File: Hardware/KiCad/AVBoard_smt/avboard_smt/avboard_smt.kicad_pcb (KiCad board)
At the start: 4 copper layers, 177.8 x 152.1 mm, 111 parts, among them IC2_AUD0 7432N, IC36 4040N, IC37 7430N, IC39 7400N, IC40 4040N, IC41 7400N, IC43 7400N, IC44 7486N, IC45 7400N, IC46 74257N, IC47 74257N, IC48 74564N, IC4_AUD0 7400N, IC53 7404N, IC6_AUD0 7474N, IC7_AUD0 LM358N, J1 5V, J2 VID_TO_MOBO, U1 W65C02SP, U2 THS7374

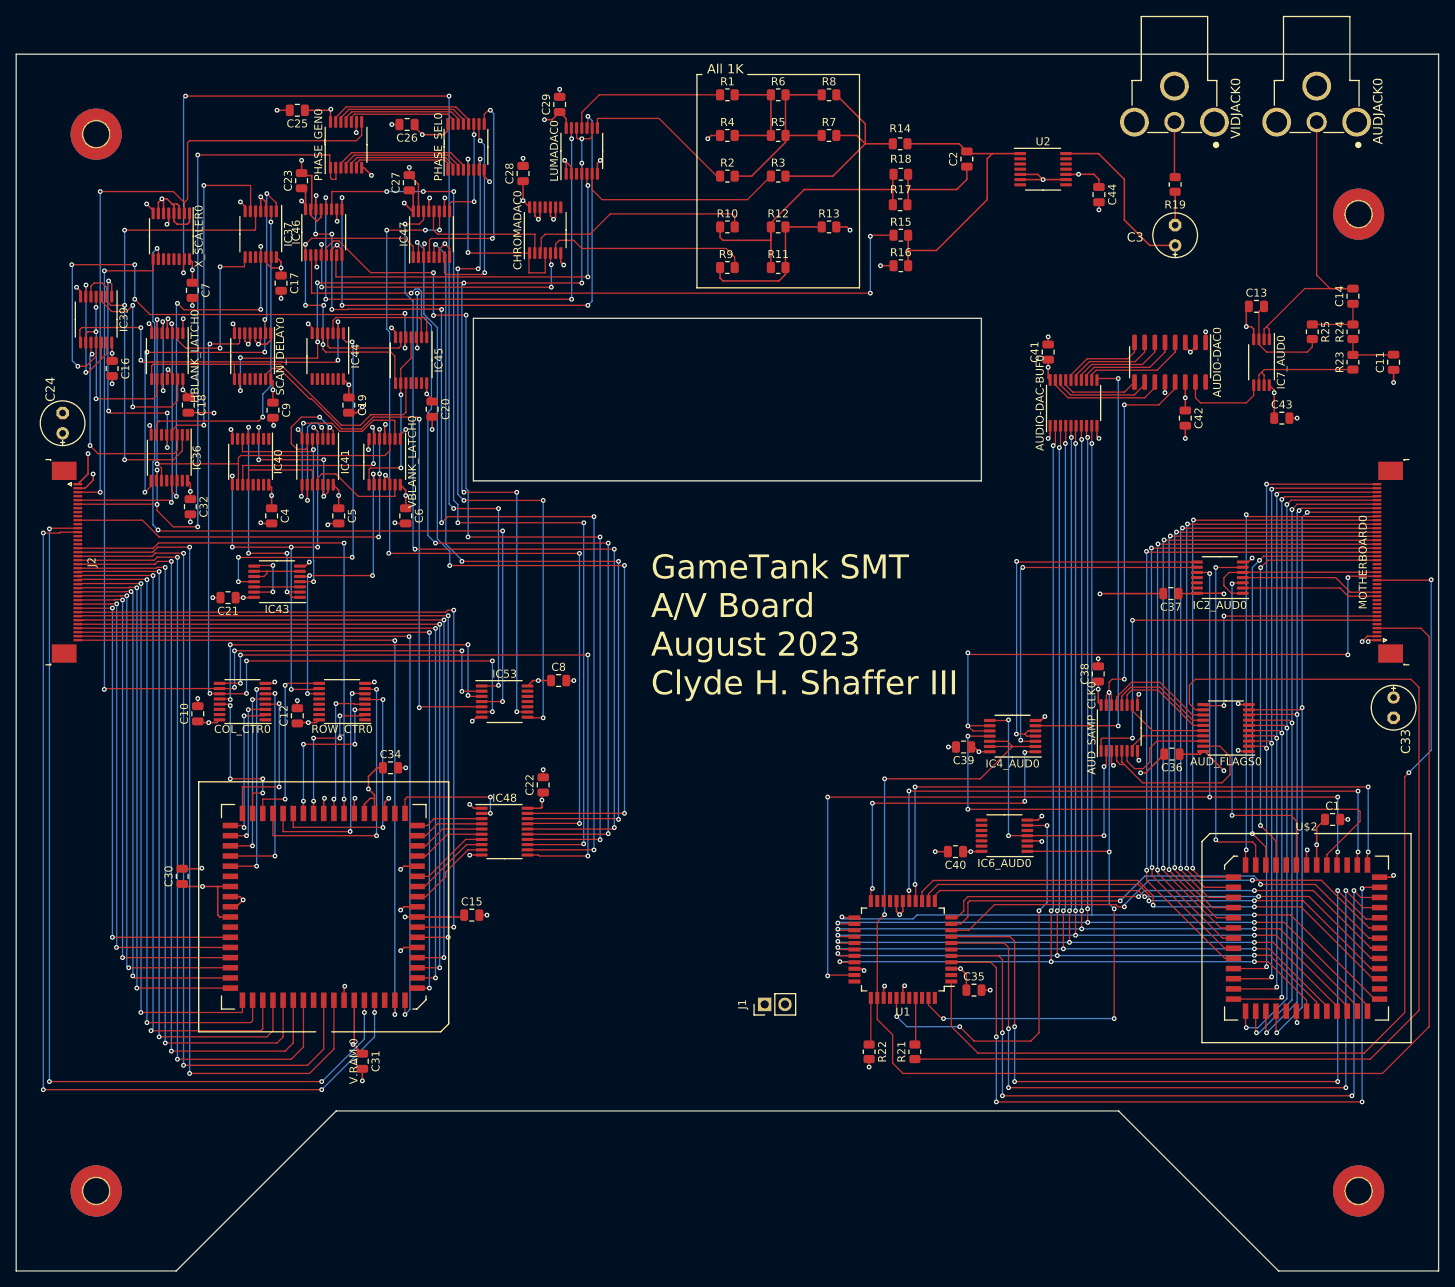
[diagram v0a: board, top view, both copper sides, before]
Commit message: SMT edits and start of fake dual ram sketching
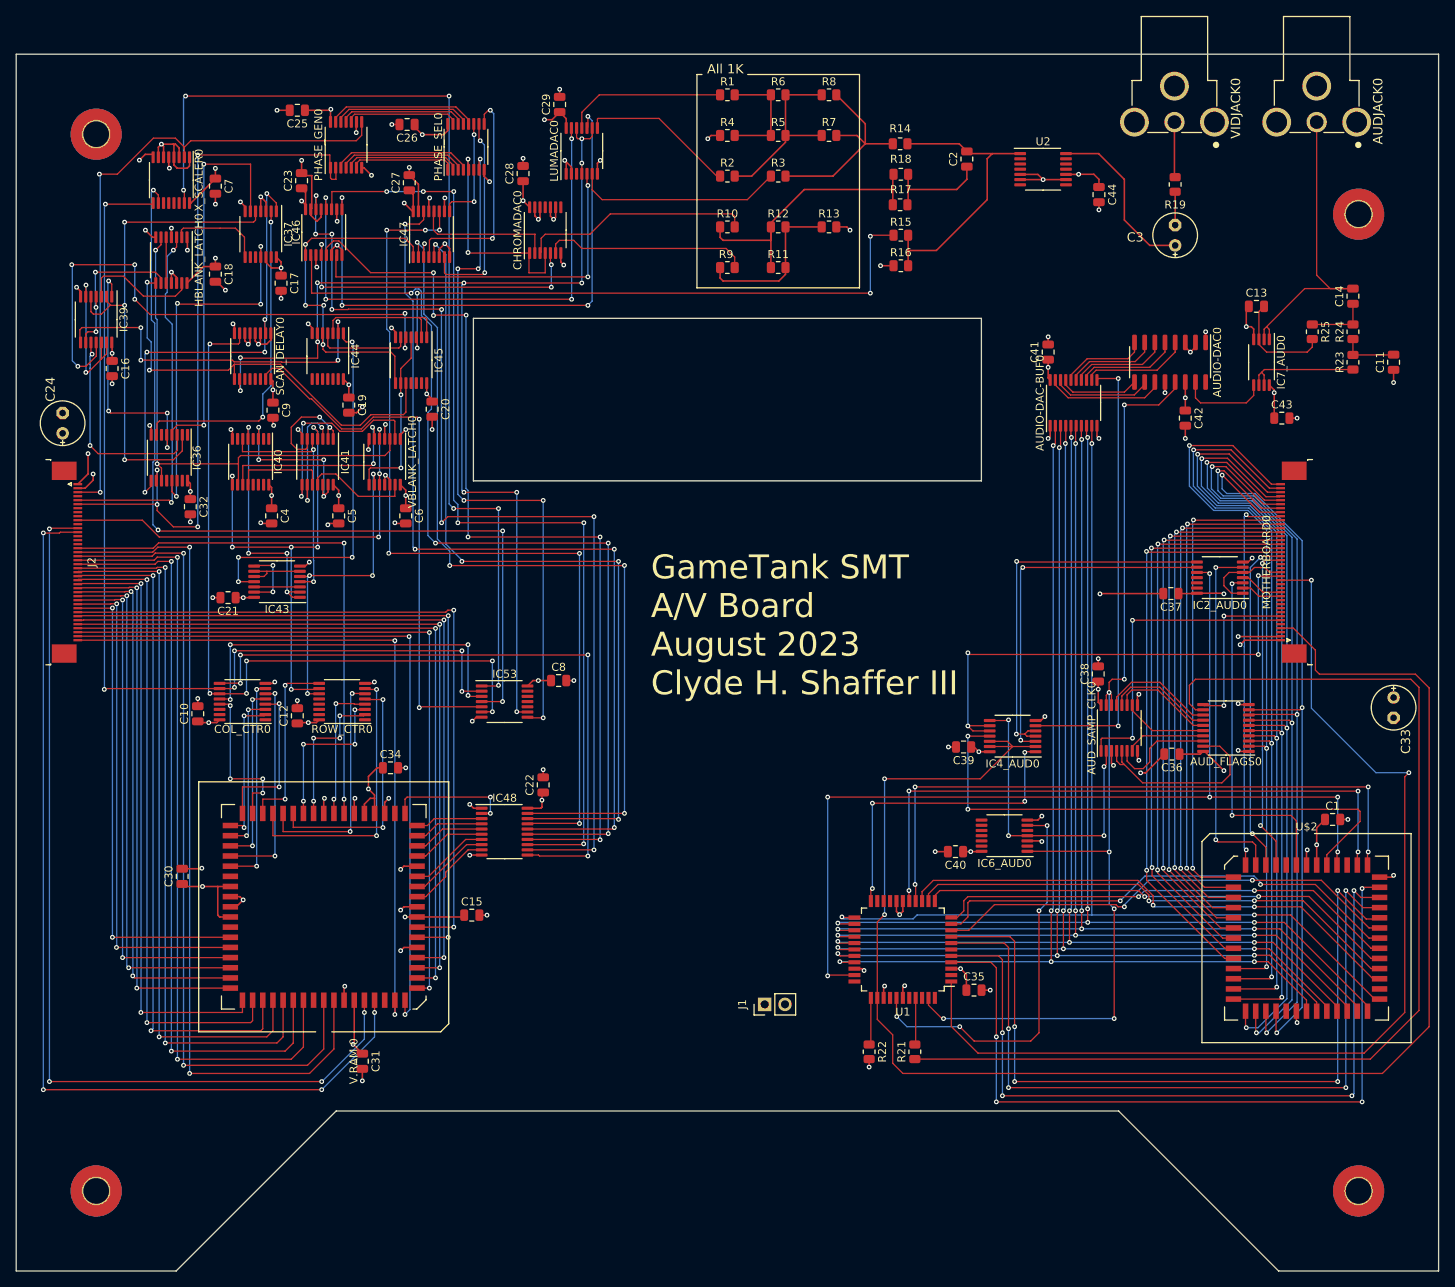
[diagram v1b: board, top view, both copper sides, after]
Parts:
- moved C18 16.7 mm to (84.5, 69.0)
- moved C7 13.3 mm to (84.5, 58.0)
- moved MOTHERBOARD0 12.1 mm to (219.0, 105.0)
- moved HBLANK_LATCH0 12.0 mm to (79.0, 67.2)
- moved X_SCALER0 7.01 mm to (79.0, 57.2)
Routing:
- net /signals_4/AUD_REG6: track 33.0 -> 21.0 mm
- net Net-(U$2B-AL9): track 84.9 -> 72.8 mm
- net Net-(U$2B-AL8): track 83.1 -> 71.1 mm
- net Net-(U$2B-AL7): track 81.4 -> 69.3 mm
- net Net-(U$2B-AL6): track 79.7 -> 67.7 mm
- net Net-(U$2B-AL4): track 76.7 -> 64.6 mm
- net Net-(U$2B-AL3): track 75.2 -> 63.1 mm
- net Net-(U$2B-AL2): track 73.7 -> 61.7 mm
- net Net-(U$2B-AL1): track 72.2 -> 60.1 mm
- net /signals_4/CLK3_5_AUD: track 50.8 -> 38.7 mm
- net /signals_4/~{RE2}: track 17.5 -> 5.48 mm
- net /signals_4/~{WE2}: track 17.2 -> 5.15 mm
- net Net-(U$2B-AL5): track 78.2 -> 66.2 mm
- net /signals_4/AUD_REG0: track 75.8 -> 63.9 mm
- net Net-(U$2B-AL11): track 52.9 -> 41.1 mm
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
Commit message: updates to kicad smt versions
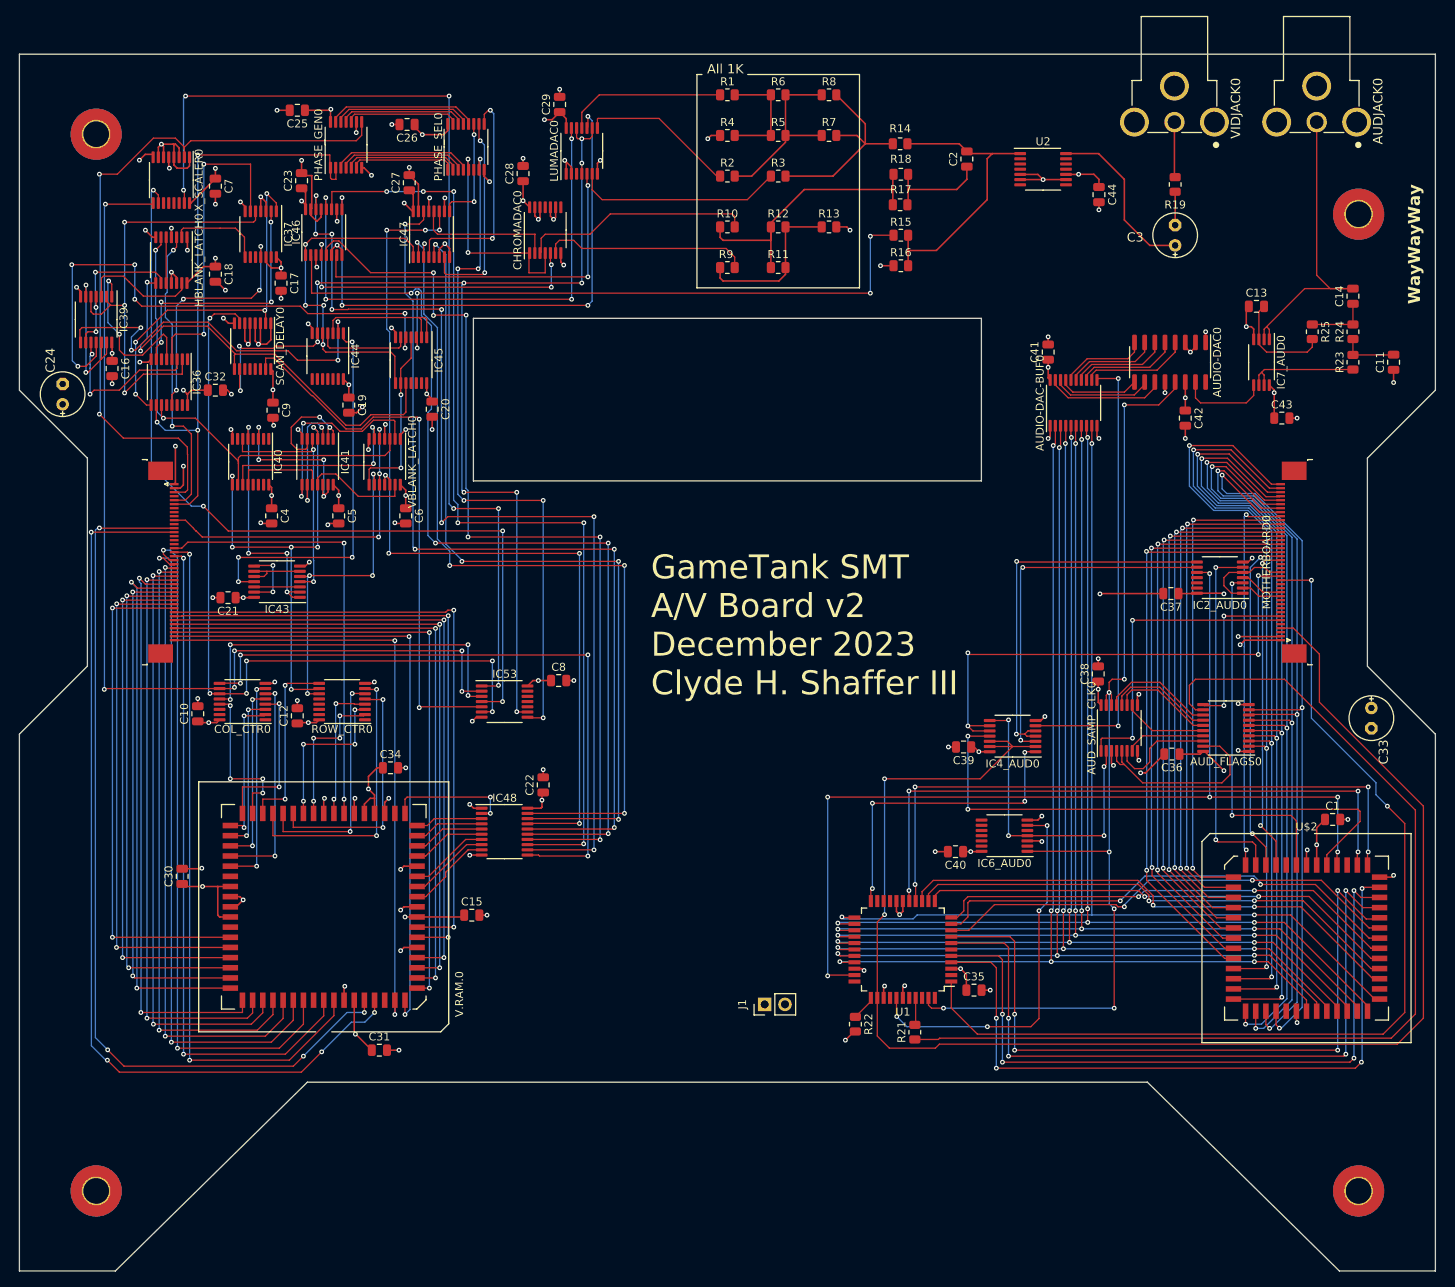
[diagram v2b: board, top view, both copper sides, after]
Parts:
- moved C32 14.9 mm to (84.5, 83.5), turned to 0 degrees
- moved J2 12.0 mm to (78.0, 105.0)
- moved IC36 9.45 mm to (78.7, 82.5)
- moved R22 3.86 mm to (164.5, 162.8)
- moved C24 3.63 mm to (65.4, 84.0)
- moved C33 3.07 mm to (229.0, 124.5)
- moved C31 2.54 mm to (105.0, 166.0), turned to 0 degrees
- moved R21 2.45 mm to (171.9, 163.8)
- moved SCAN_DELAY0 1.25 mm to (89.2, 78.0)
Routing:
- net /Composite Video Generator/VA14: track 105.4 -> 87.6 mm
- net /Composite Video Generator/VA13: track 101.9 -> 84.7 mm
- net /Composite Video Generator/CLK3_5: track 90.1 -> 75.2 mm, vias 4 -> 3
- net /Composite Video Generator/256H: track 45.4 -> 30.7 mm
- net /Composite Video Generator/2H: track 58.4 -> 45.9 mm, vias 5 -> 4
- net /Composite Video Generator/VA10: track 90.1 -> 77.7 mm
- net /signals_4/CLK14_AUD: track 198.7 -> 186.6 mm
- net /Composite Video Generator/VD5: track 91.3 -> 79.3 mm
- net /Composite Video Generator/VD4: track 91.5 -> 79.4 mm
- net /Composite Video Generator/VD7: track 91.3 -> 79.3 mm
- net /Composite Video Generator/VD3: track 90.7 -> 78.7 mm
- net /Composite Video Generator/VD2: track 90.0 -> 77.9 mm
- net /Composite Video Generator/VD1: track 90.8 -> 78.7 mm
- net /Composite Video Generator/VD0: track 88.2 -> 76.1 mm
- net /Composite Video Generator/~{VRESET}: track 54.6 -> 42.5 mm
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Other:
- board size 177.8 x 152.1 mm -> 177 x 152.1 mm
- board text added: "GameTank SMT A/V Board v2 December 2023 Clyde H. Shaffer III"
- board text added: "WayWayWay"
- board text removed: "GameTank SMT A/V Board August 2023 Clyde H. Shaffer III"

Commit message: collect production documents for quoting
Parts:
- J2, MOTHERBOARD0: footprint Connector_FFC-FPC:TE_4-1734839-0_1x40-1MP_P0.5mm_Horizontal -> SamacSys_Parts:F34G1A7Q1E8C40
- moved J2 1.00 mm to (77.0, 105.0)
- moved MOTHERBOARD0 1.00 mm to (220.0, 105.0)
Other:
- board text added: "GameTank SMT A/V Board v3 September 2025 Clyde H. Shaffer III"
- board text removed: "GameTank SMT A/V Board v2 December 2023 Clyde H. Shaffer III"
